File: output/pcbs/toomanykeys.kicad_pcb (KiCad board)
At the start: 2 copper layers, 156.8 x 117.1 mm, 80 parts

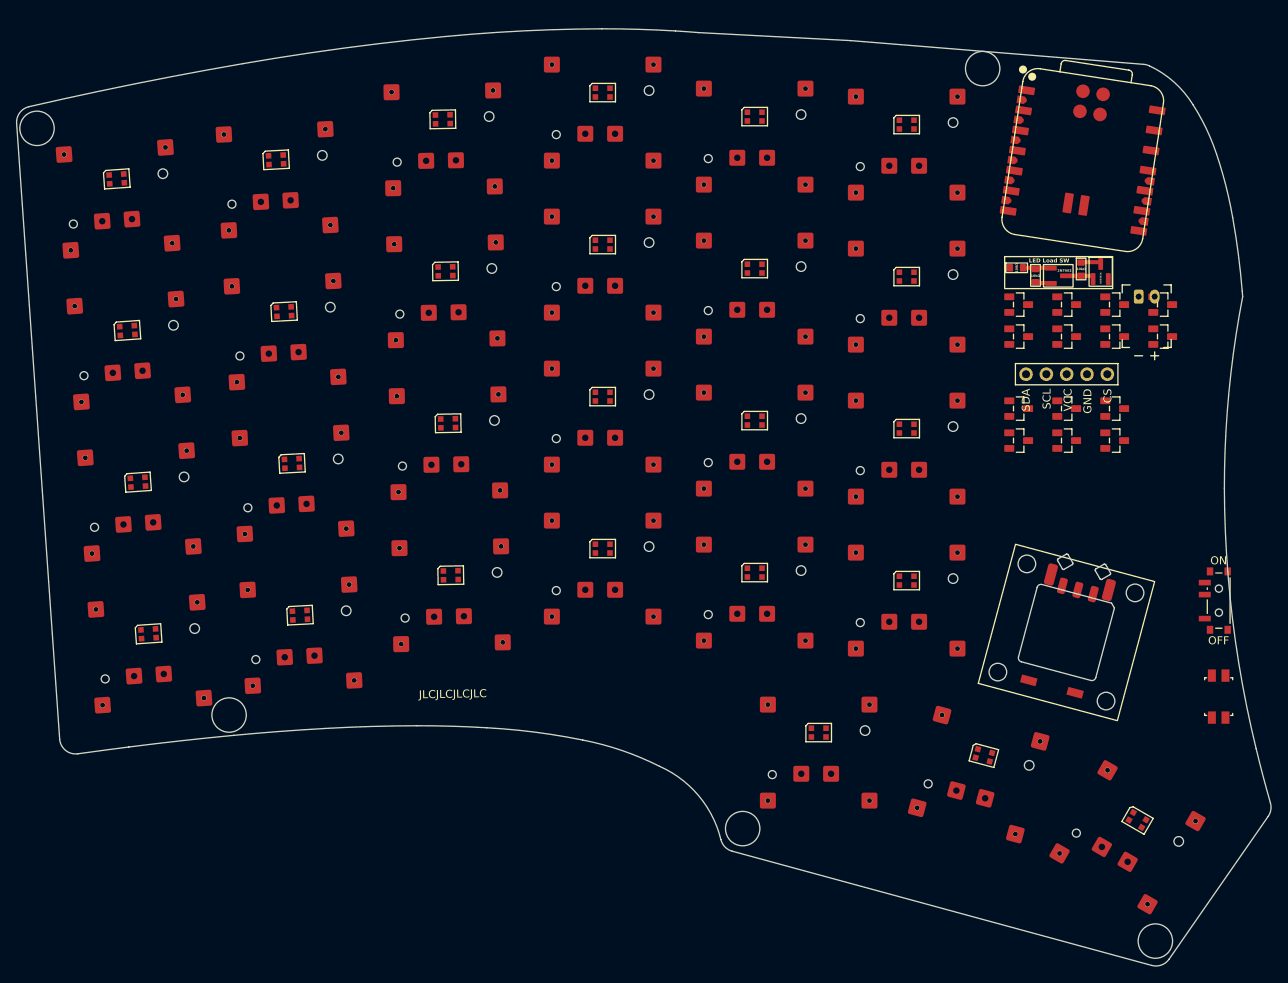
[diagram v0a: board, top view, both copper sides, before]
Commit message: Add nets to MCU, fix diode assignments, work on LEDs.
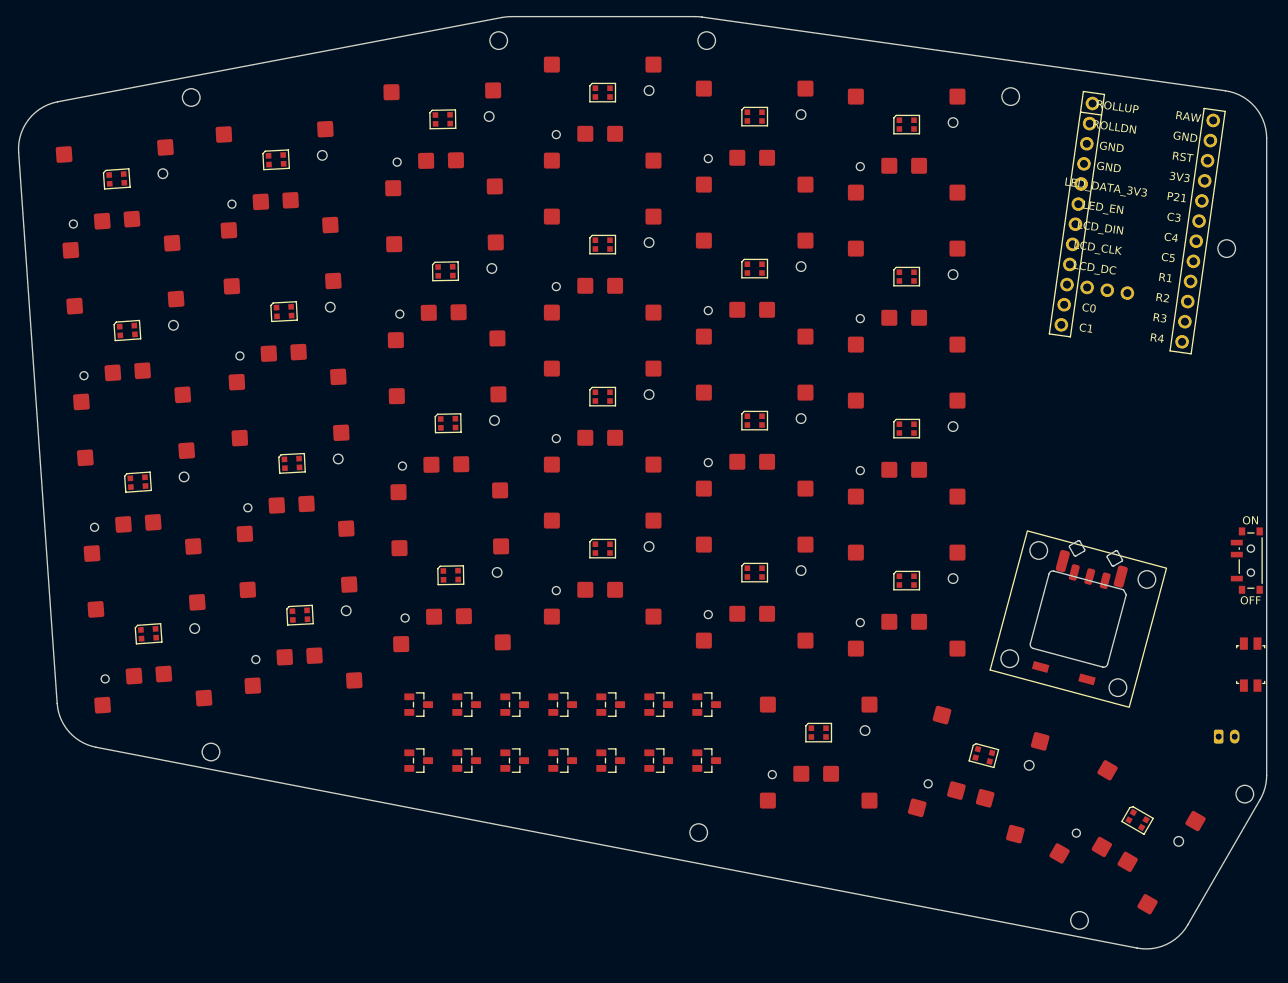
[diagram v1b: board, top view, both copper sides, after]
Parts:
- removed DISP1: , ceoloide:display_nice_view
- removed XX1: , LED_Load_SW
- added MH6: , ceoloide:mounting_hole_npth, F.Cu at (194.6, 109.4)
- added MH7: , ceoloide:mounting_hole_npth, F.Cu at (128.6, 182.4)
- added MH8: , ceoloide:mounting_hole_npth, F.Cu at (176.2, 193.3)
- added MH9: , ceoloide:mounting_hole_npth, F.Cu at (196.9, 177.5)
- JST1: moved to B.Cu
- MCU1: footprint XIAO-nRF52840-Plus-SMD -> ceoloide:mcu_nice_nano
- moved MH5 107.1 mm to (167.6, 90.4), turned to 0 degrees
- moved MH4 98.6 mm to (129.6, 83.4)
- moved D8 92.2 mm to (93.6, 173.4)
- moved D9 92.2 mm to (99.6, 173.4)
- moved D1 90.1 mm to (93.6, 166.4)
- moved D2 90.1 mm to (99.6, 166.4)
- moved D3 90.1 mm to (105.6, 166.4)
- moved D13 85.0 mm to (123.6, 173.4)
- moved D14 77.8 mm to (129.6, 173.4)
- moved D10 74.6 mm to (105.6, 173.4)
- moved D11 74.6 mm to (111.6, 173.4)
- moved D12 74.6 mm to (117.6, 173.4)
- moved D4 73.2 mm to (111.6, 166.4)
- moved D5 73.2 mm to (117.6, 166.4)
- moved D6 73.2 mm to (123.6, 166.4)
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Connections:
- net CLK renamed LCD_CS
- net LED_START renamed LED_DATA_5V
- net P0.04 renamed P21
- net P0.09 renamed LCD_DIN
- net P0.10 renamed LED_EN
- net P0.15 renamed LCD_BL
- net P0.19 renamed LCD_DC
- net P0.31 renamed LED_DATA_3V3
- net P1.01 renamed LCD_CLK
- net P1.14 renamed R2
- net P1.15 renamed R3
- MCU1 pad 1: P0.02 -> RAW
- MCU1 pad 12: 3V3 -> R4
- MCU1 pad 13: GND -> C1
- MCU1 pad 14: 5V -> C0
- MCU1 pad 2: P0.03 -> GND
- MCU1 pad 21: P1.03 -> GND
- MCU1 pad 22: P1.05 -> GND
- MCU1 pad 23: P1.07 -> ROLLDN
- MCU1 pad 24: DIO -> ROLLUP
- MCU1 pad 26: RST -> LCD_RST
- MCU1 pad 27: GND -> C2
- MCU1 pad 3: P0.28 -> RST
- MCU1 pad 4: P0.29 -> 3V3
- MCU1 pad 6: P0.05 -> C3
- MCU1 pad 7: P1.11 -> C4
- MCU1 pad 8: P1.12 -> C5
- MCU1 pad 9: P1.13 -> R1
- RE1 pad A: ENC_UP -> ROLLUP
- RE1 pad C: ENC_DN -> ROLLDN
- S1 pad : finger_outer_bottom -> (no net)
- S1 pad 3: (no net) -> GND
- S10 pad : finger_ring_home -> (no net)
- S10 pad 3: (no net) -> GND
- S11 pad : finger_ring_top -> (no net)
- S11 pad 3: (no net) -> GND
- S12 pad : finger_ring_num -> (no net)
- S12 pad 3: (no net) -> GND
- S13 pad : finger_middle_bottom -> (no net)
- S13 pad 3: (no net) -> GND
- S14 pad : finger_middle_home -> (no net)
- S14 pad 3: (no net) -> GND
- S15 pad : finger_middle_top -> (no net)
- S15 pad 3: (no net) -> GND
- S16 pad : finger_middle_num -> (no net)
- S16 pad 3: (no net) -> GND
- S17 pad : finger_index_bottom -> (no net)
- S17 pad 3: (no net) -> GND
- S18 pad : finger_index_home -> (no net)
- S18 pad 3: (no net) -> GND
- S19 pad : finger_index_top -> (no net)
- S19 pad 3: (no net) -> GND
- S2 pad : finger_outer_home -> (no net)
- S2 pad 3: (no net) -> GND
- S20 pad : finger_index_num -> (no net)
- S20 pad 3: (no net) -> GND
- S21 pad : finger_inner_bottom -> (no net)
- S21 pad 3: (no net) -> GND
- S22 pad : finger_inner_home -> (no net)
- S22 pad 3: (no net) -> GND
- S23 pad : finger_inner_top -> (no net)
- S23 pad 3: (no net) -> GND
- S24 pad : finger_inner_num -> (no net)
- S24 pad 3: (no net) -> GND
- S25 pad : thumb_near_fan -> (no net)
- S25 pad 3: (no net) -> GND
- S26 pad : thumb_mid_fan -> (no net)
- S26 pad 3: (no net) -> GND
- S27 pad : thumb_far_fan -> (no net)
- S27 pad 3: (no net) -> GND
- S3 pad : finger_outer_top -> (no net)
- S3 pad 3: (no net) -> GND
- S4 pad : finger_outer_num -> (no net)
- S4 pad 3: (no net) -> GND
- S5 pad : finger_pinky_bottom -> (no net)
- S5 pad 3: (no net) -> GND
- S6 pad : finger_pinky_home -> (no net)
- S6 pad 3: (no net) -> GND
- S7 pad : finger_pinky_top -> (no net)
- S7 pad 3: (no net) -> GND
- S8 pad : finger_pinky_num -> (no net)
- S8 pad 3: (no net) -> GND
- S9 pad : finger_ring_bottom -> (no net)
- S9 pad 3: (no net) -> GND
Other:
- board size 156.8 x 117.1 mm -> 156 x 116.5 mm
- board text removed: "JLCJLCJLCJLC"

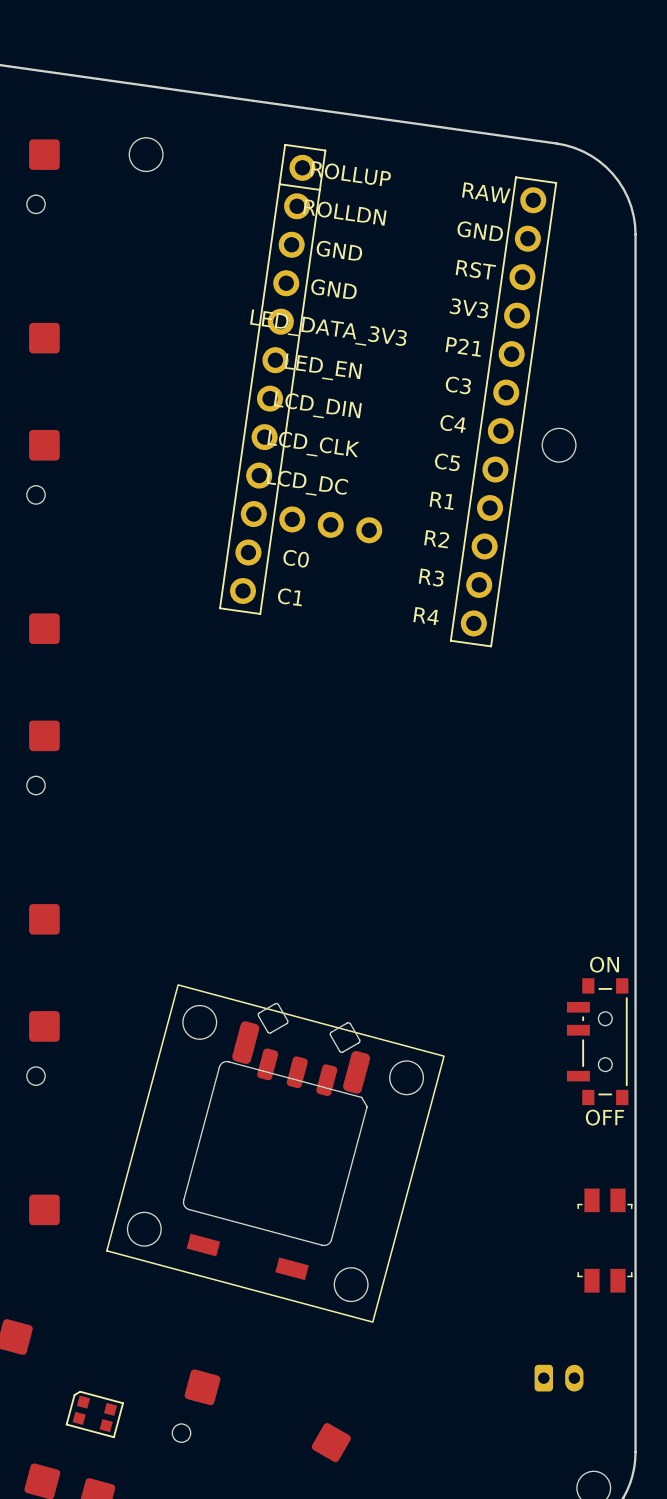
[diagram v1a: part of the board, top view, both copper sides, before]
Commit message: Complete draft 3 of routing, near complete. Fix pad positions on roller encoder.
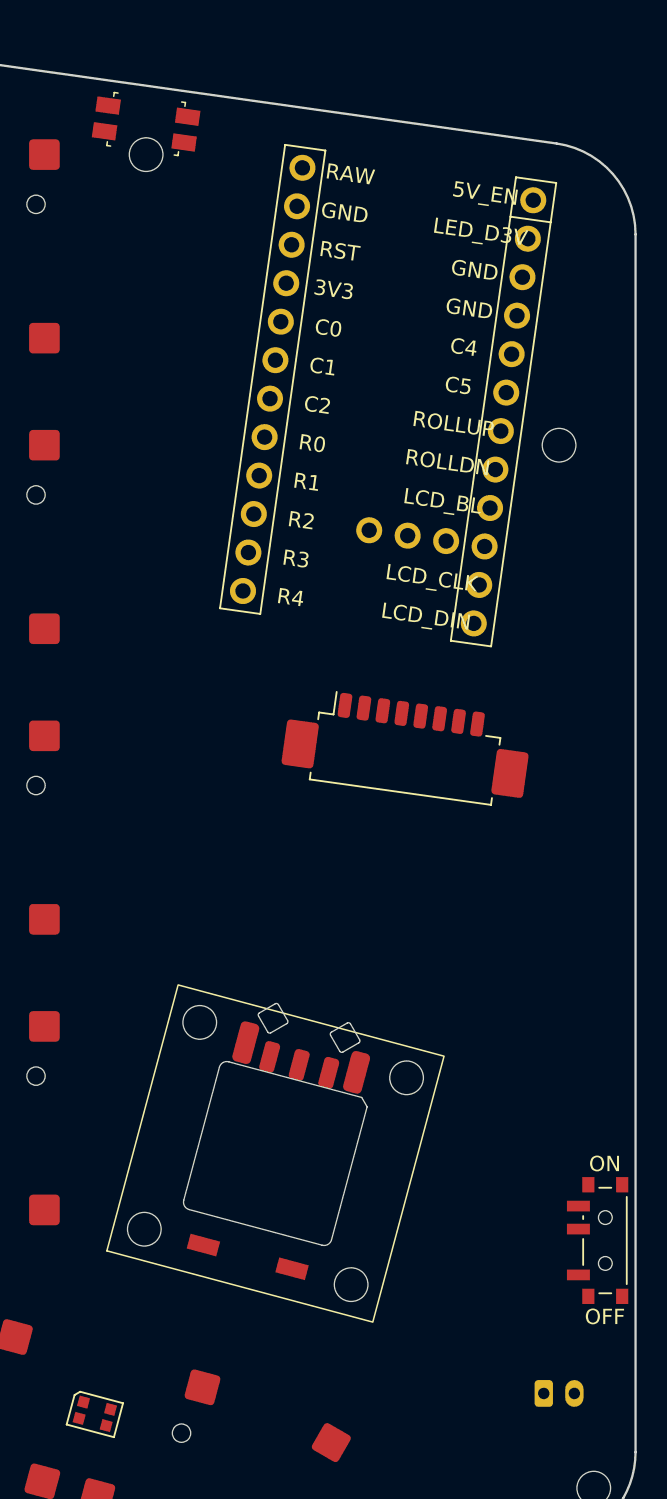
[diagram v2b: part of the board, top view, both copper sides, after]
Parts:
- added CONN1: , Molex_PicoBlade_53261-0871_1x08-1MP_P1.25mm_Horizontal, F.Cu at (184.6, 129.4)
- moved RST1 78.9 mm to (167.6, 88.4), turned to -8 degrees
- moved D7 36.7 mm to (93.6, 173.4)
- moved PWR1 13.0 mm to (197.6, 161.4)
- moved D13 9.22 mm to (129.6, 166.4)
- moved D10 6.00 mm to (111.6, 173.4)
- moved D11 6.00 mm to (117.6, 173.4)
- moved D12 6.00 mm to (123.6, 173.4)
- moved D8 6.00 mm to (99.6, 173.4)
- moved D9 6.00 mm to (105.6, 173.4)
- moved JST1 1.00 mm to (194.6, 171.4)
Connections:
- net LED_DATA_5V renamed LED_D5V
- net LED_PWR renamed 5V
- D1 pad 1: finger_outer_num -> finger_pinky_num
- D1 pad 2: finger_pinky_num -> finger_outer_num
- D1 pad 3: R1 -> R0
- D10 pad 1: finger_outer_bottom -> finger_pinky_bottom
- D10 pad 3: R1 -> R3
- D11 pad 1: finger_ring_bottom -> finger_middle_bottom
- D11 pad 2: finger_middle_bottom -> finger_ring_bottom
- D11 pad 3: R1 -> R3
- D12 pad 1: finger_index_bottom -> finger_inner_bottom
- D12 pad 2: finger_inner_bottom -> finger_index_bottom
- D12 pad 3: R1 -> R3
- D13 pad 1: thumb_near_fan -> roller
- D13 pad 2: thumb_mid_fan -> thumb_near_fan
- D13 pad 3: R1 -> R4
- D14 pad 1: thumb_far_fan -> thumb_mid_fan
- D14 pad 2: roller -> thumb_far_fan
- D14 pad 3: R1 -> R4
- D2 pad 1: finger_ring_num -> finger_middle_num
- D2 pad 2: finger_middle_num -> finger_ring_num
- D2 pad 3: R1 -> R0
- D3 pad 1: finger_index_num -> finger_inner_num
- D3 pad 2: finger_inner_num -> finger_index_num
- D3 pad 3: R1 -> R0
- D4 pad 1: finger_outer_top -> finger_pinky_top
- D5 pad 1: finger_ring_top -> finger_middle_top
- D5 pad 2: finger_middle_top -> finger_ring_top
- D6 pad 1: finger_index_top -> finger_inner_top
- D6 pad 2: finger_inner_top -> finger_index_top
- D7 pad 1: finger_outer_home -> finger_pinky_home
- D7 pad 3: R1 -> R2
- D8 pad 1: finger_ring_home -> finger_middle_home
- D8 pad 2: finger_middle_home -> finger_ring_home
- D8 pad 3: R1 -> R2
- D9 pad 1: finger_index_home -> finger_inner_home
- D9 pad 2: finger_inner_home -> finger_index_home
- D9 pad 3: R1 -> R2
- MCU1 pad 1: RAW -> 5V_EN
- MCU1 pad 10: R2 -> LCD_DC
- MCU1 pad 11: R3 -> LCD_CLK
- MCU1 pad 12: R4 -> LCD_DIN
- MCU1 pad 13: C1 -> R4
- MCU1 pad 14: C0 -> R3
- MCU1 pad 15: LCD_BL -> R2
- MCU1 pad 16: LCD_DC -> R1
- MCU1 pad 17: LCD_CLK -> R0
- MCU1 pad 18: LCD_DIN -> C2
- MCU1 pad 19: LED_EN -> C1
- MCU1 pad 2: GND -> LED_D3V
- MCU1 pad 20: LED_DATA_3V3 -> C0
- MCU1 pad 21: GND -> 3V3
- MCU1 pad 22: GND -> RST
- MCU1 pad 23: ROLLDN -> GND
- MCU1 pad 24: ROLLUP -> RAW
- MCU1 pad 25: LCD_CS -> LCD_RST
- MCU1 pad 26: LCD_RST -> LCD_CS
- MCU1 pad 27: C2 -> C3
- MCU1 pad 3: RST -> GND
- MCU1 pad 4: 3V3 -> GND
- MCU1 pad 5: P21 -> C4
- MCU1 pad 6: C3 -> C5
- MCU1 pad 7: C4 -> ROLLUP
- MCU1 pad 8: C5 -> ROLLDN
- MCU1 pad 9: R1 -> LCD_BL
- PWR1 pad 2: RAW -> BAT_P
- PWR1 pad 3: BAT_P -> RAW

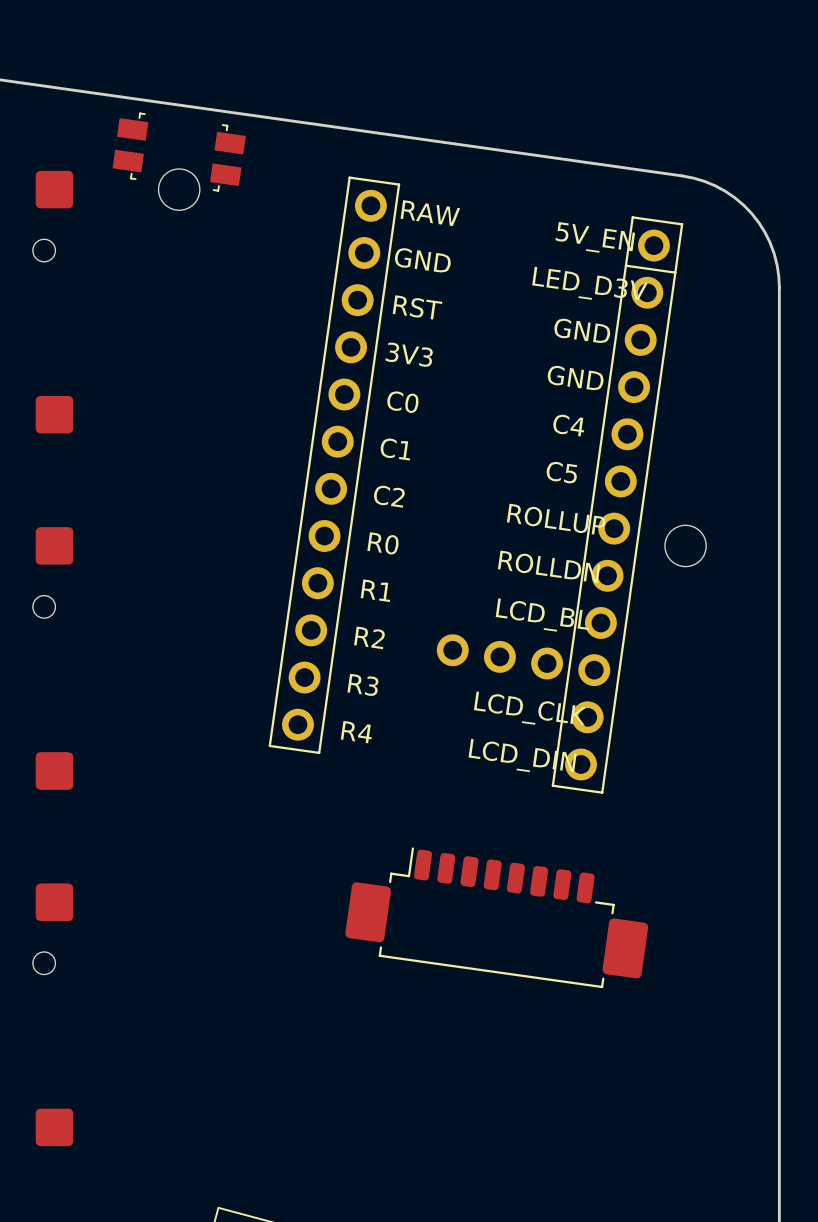
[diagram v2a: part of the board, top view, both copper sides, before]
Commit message: Add LCD outline to board, move other components as needed. Add 3D model support to several footprints, add model for CKW12 roller encoder.
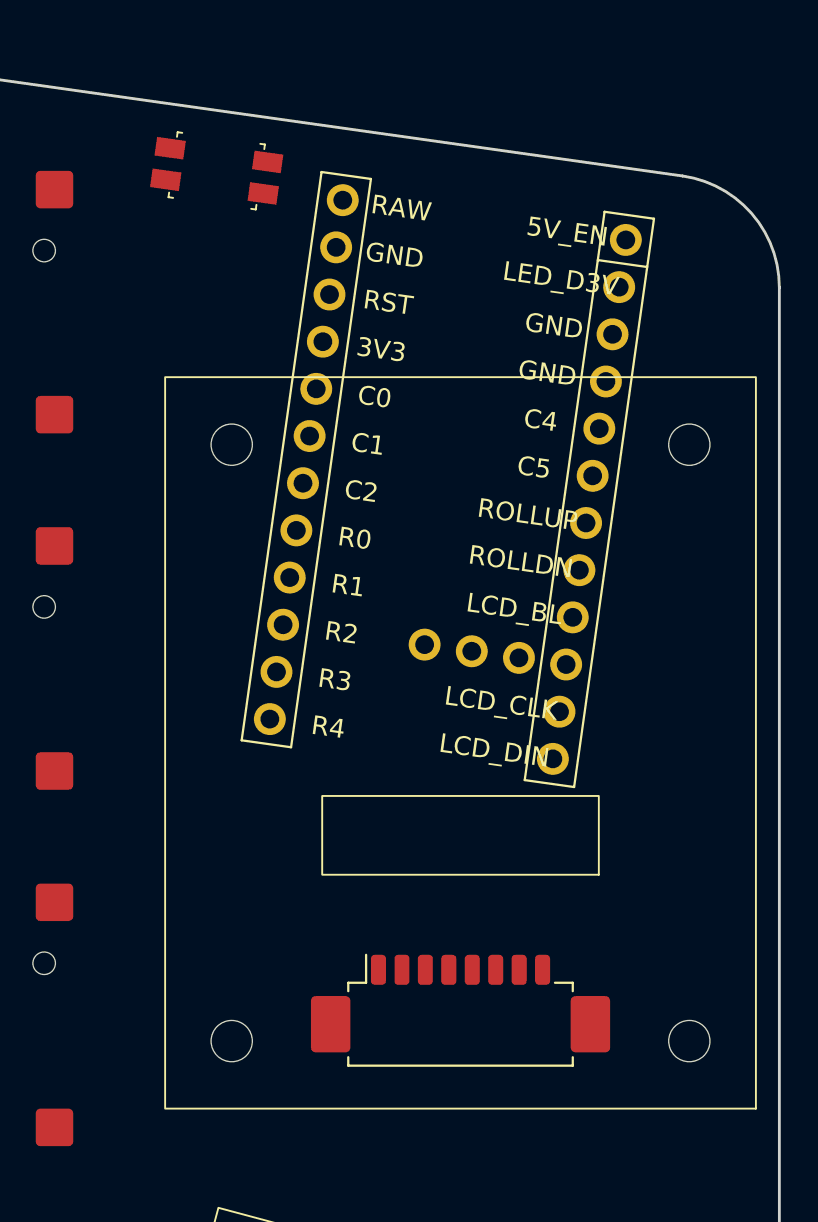
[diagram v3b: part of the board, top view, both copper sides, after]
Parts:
- removed MH8, MH9: , ceoloide:mounting_hole_npth
- added LCD1: , LCD_1.69_Waveshare, F.Cu at (182.6, 119.9)
- moved MH5 99.9 mm to (128.6, 182.4)
- moved MH6 86.0 mm to (176.2, 193.3), turned to -30 degrees
- moved MH7 68.4 mm to (196.9, 177.5), turned to -30 degrees
- moved D1 7.00 mm to (93.6, 173.4)
- moved D10 7.00 mm to (111.6, 166.4)
- moved D11 7.00 mm to (117.6, 166.4)
- moved D12 7.00 mm to (123.6, 166.4)
- moved D2 7.00 mm to (99.6, 173.4)
- moved D3 7.00 mm to (105.6, 173.4)
- moved D4 7.00 mm to (111.6, 173.4)
- moved D5 7.00 mm to (117.6, 173.4)
- moved D6 7.00 mm to (123.6, 173.4)
- moved D7 7.00 mm to (93.6, 166.4)
- moved D8 7.00 mm to (99.6, 166.4)
- moved D9 7.00 mm to (105.6, 166.4)
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
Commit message: Fix whatever boneheaded thing I did to mess up all the boostier pads.
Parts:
- moved JST1 0.27 mm to (194.9, 171.4)
